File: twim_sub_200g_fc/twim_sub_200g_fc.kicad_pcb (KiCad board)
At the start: 2 copper layers, 37 x 25 mm, 41 parts, among them J1 GNSS_1, J2 GNSS_2, J3 ELRS, J4 BATTERY CONNECTOR, J5 SWD CONN, J7 VTX_CONN, J8 USB_CONN, M1 Motor_Servo, M2 Motor_Servo, M3 Motor_Servo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

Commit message: qsss
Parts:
- U1: moved to B.Cu
- moved U3 25.2 mm to (111.5, 40.8)
- moved U5 19.4 mm to (111.8, 36.9)
- moved U4 11.2 mm to (125.0, 37.6)
- moved M1 8.81 mm to (128.9, 30.0)
- moved M2 8.81 mm to (128.9, 33.6)
- moved M3 8.81 mm to (128.9, 26.4)
- moved M4 8.81 mm to (128.9, 22.8)
- moved J4 8.05 mm to (125.9, 41.0)
- moved J2 8.01 mm to (132.0, 41.0)
- moved J8 6.43 mm to (119.0, 39.0)
- moved U1 3.36 mm to (120.8, 28.0), turned to -90 degrees
- moved J5 1.40 mm to (116.0, 19.3)
- moved J1 0.38 mm to (124.0, 19.0), turned to 0 degrees
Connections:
- U1 pad 2: PWM_3 -> PWM_4
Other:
- board size 37 x 25 mm -> 27 x 25 mm

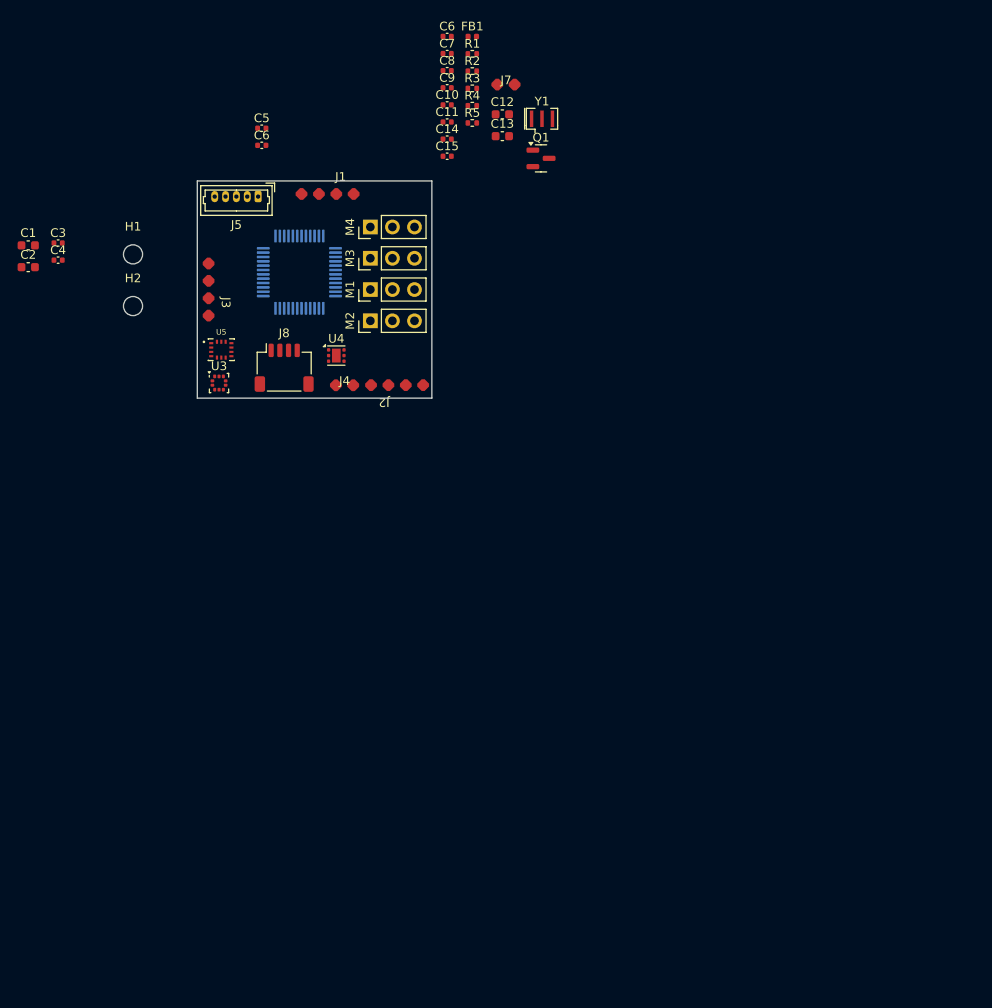
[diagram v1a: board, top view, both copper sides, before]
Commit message: added main layout 22mmx30mm
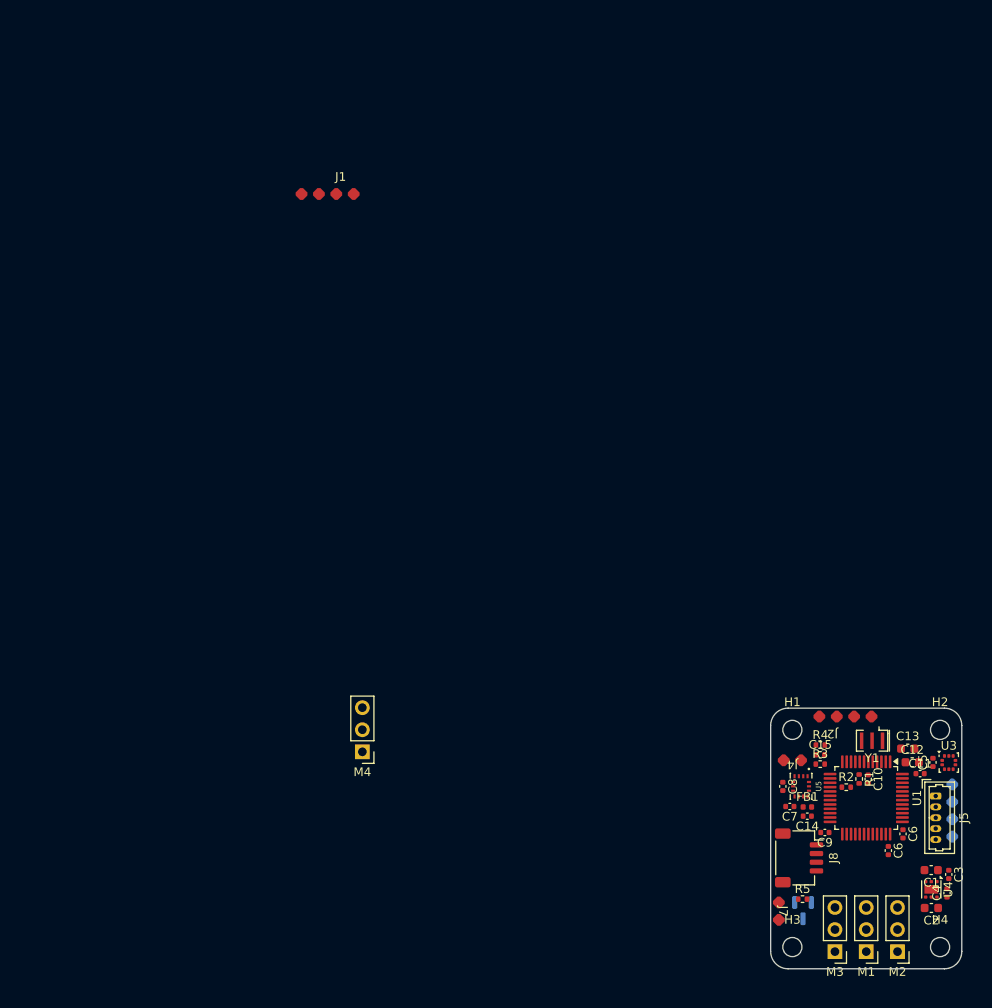
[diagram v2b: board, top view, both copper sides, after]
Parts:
- added H3: MountingHole, MountingHole:MountingHole_2.2mm_M2, F.Cu at (177.5, 105.7)
- added H4: MountingHole, MountingHole:MountingHole_2.2mm_M2, F.Cu at (194.5, 105.7)
- J3, Q1: moved to B.Cu
- U1: moved to F.Cu
- moved C2 127.5 mm to (193.5, 101.2), turned to 180 degrees
- moved C1 126.4 mm to (193.5, 96.8), turned to 180 degrees
- moved C3 125.7 mm to (195.5, 97.3), turned to -90 degrees
- moved C4 125.6 mm to (195.3, 99.5), turned to 90 degrees
- moved C6 108.3 mm to (190.2, 92.7), turned to -90 degrees
- moved C6 106.6 mm to (188.5, 94.6), turned to -90 degrees
- moved C5 106.3 mm to (193.7, 84.4), turned to 90 degrees
- moved H2 104.9 mm to (194.5, 80.7)
- moved J3 104.6 mm to (195.9, 90.0)
- moved J5 104.1 mm to (194.0, 88.3), turned to -90 degrees
- moved J7 100.2 mm to (175.9, 101.6), turned to -90 degrees
- moved R5 97.1 mm to (178.7, 100.2)
- moved FB1 96.7 mm to (179.2, 89.6)
- moved C9 96.1 mm to (181.2, 92.5), turned to 180 degrees
- moved M3 96.1 mm to (182.4, 106.2), turned to 180 degrees
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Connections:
- J2 pad 1: GNSS_2_RX -> GNSS_2_TX
- J2 pad 2: GNSS_2_TX -> GNSS_2_RX
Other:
- board size 27 x 25 mm -> 22 x 30 mm

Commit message: added baselayout
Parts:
- removed J1: GNSS_1, smd_pads:01x04_smd_pad_1.2mm
- removed M4: Motor_Servo, Connector_PinHeader_2.54mm:PinHeader_1x03_P2.54mm_Vertical
- moved J2 19.2 mm to (186.0, 98.2)
- moved C10 5.30 mm to (183.0, 82.2), turned to 90 degrees
- moved R2 4.78 mm to (188.4, 88.2), turned to 180 degrees
- moved R1 4.32 mm to (184.0, 82.2), turned to 90 degrees
- moved J5 1.89 mm to (193.9, 90.2)
- moved C6 1.46 mm to (190.0, 94.7)
- moved C1 1.14 mm to (193.5, 98.0)
- moved C4 1.14 mm to (195.3, 100.6)
- moved C2 1.14 mm to (193.5, 102.3)
- moved C3 1.14 mm to (195.5, 98.5)
- moved U4 1.14 mm to (193.5, 100.2)
- moved J3 0.83 mm to (195.6, 90.7)
- moved R5 0.57 mm to (179.2, 100.3)
- moved Q1 0.57 mm to (179.3, 101.6)
- moved J7 0.55 mm to (176.5, 101.4)
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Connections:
- U1 pad 10: GNSS_2_TX -> unconnected-(U1-PA2-Pad10)
- U1 pad 11: GNSS_2_RX -> unconnected-(U1-PA3-Pad11)
- U1 pad 2: PWM_4 -> unconnected-(U1-PC13-Pad2)
- U1 pad 31: GNSS_1_TX -> GNSS_2_TX
- U1 pad 32: GNSS_1_RX -> GNSS_2_RX
- U1 pad 8: PWM_1 -> PWM_2
- U1 pad 9: PWM_2 -> PWM_1
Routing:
- net +3V3: track 0.00 -> 74.0 mm, vias 0 -> 1
- net +5V: track 0.00 -> 40.6 mm
- net GND: track 0.00 -> 26.5 mm, vias 0 -> 13
- net PWM_2: track 0.00 -> 23.7 mm, vias 0 -> 1
- net PWM_1: track 0.00 -> 22.9 mm, vias 0 -> 1
- net NRST: track 0.00 -> 19.0 mm, vias 0 -> 1
- net VTX_ON: track 0.00 -> 17.7 mm, vias 0 -> 2
- net PWM_3: track 0.00 -> 15.2 mm, vias 0 -> 1
- net GNSS_2_TX: track 0.00 -> 12.8 mm, vias 0 -> 2
- net USB_DP: track 0.00 -> 11.2 mm, vias 0 -> 2
- net SCLK_BARO: track 0.00 -> 10.5 mm, vias 0 -> 2
- net USB_DM: track 0.00 -> 9.34 mm
- net GNSS_2_RX: track 0.00 -> 8.89 mm, vias 0 -> 2
- net BAT_VOLTAGE_ADC: track 0.00 -> 8.20 mm, vias 0 -> 2
- net CS_BARO: track 0.00 -> 7.78 mm
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- added copper zone on B.Cu, net GND
- added copper zone on F.Cu, net GND
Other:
- copper layers 2 -> 4

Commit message: adddd
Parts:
- removed Q1: AO3400A, Package_TO_SOT_SMD:SOT-23
- removed U4: TLV75533PDRV, Package_SON:WSON-6-1EP_2x2mm_P0.65mm_EP1x1.6mm
- added Q2: DMG1012T, Package_TO_SOT_SMD:SOT-523, F.Cu at (178.2, 101.3)
- added U2: AP2112K-3.3, PCM_SparkFun-Semiconductor-Standard:SOT23-5, F.Cu at (193.1, 99.5)
- moved R2 3.85 mm to (192.1, 87.2), turned to 0 degrees
- moved C1 2.69 mm to (190.8, 97.8), turned to -90 degrees
- moved R5 1.28 mm to (179.9, 101.4), turned to 90 degrees
- moved C4 1.12 mm to (195.0, 101.7)
- moved C6 0.75 mm to (189.3, 94.4), turned to 0 degrees
- moved C2 0.50 mm to (193.0, 102.4)
- moved C3 0.41 mm to (195.1, 98.4)
- moved C14 0.33 mm to (179.5, 90.8), turned to 180 degrees
- moved C11 0.24 mm to (192.1, 85.7)
- moved FB1 0.12 mm to (179.2, 89.7)
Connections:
- J2 pad 1: GNSS_2_TX -> GNSS_2_RX
- J2 pad 2: GNSS_2_RX -> GNSS_2_TX
- J3 pad 3: +5V -> GND
- J3 pad 4: GND -> +5V
- U1 pad 17: unconnected-(U1-PB1-Pad17) -> INT_DR_IMU_1
- U1 pad 18: unconnected-(U1-PB2-Pad18) -> INT_DR_IMU_2
- U1 pad 2: unconnected-(U1-PC13-Pad2) -> INT_DR_BARO
- U1 pad 25: unconnected-(U1-PB11-Pad25) -> VTX_ON
- U1 pad 39: VTX_ON -> unconnected-(U1-PA15-Pad39)
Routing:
- net +3V3: track 74.0 -> 34.9 mm, vias 1 -> 20
- net GND: track 26.5 -> 49.1 mm, vias 13 -> 31
- net +5V: track 40.6 -> 57.3 mm, vias 0 -> 9
- net INT_DR_BARO: track 0.00 -> 12.6 mm
- net INT_DR_IMU_1: track 0.00 -> 7.42 mm, vias 0 -> 2
- net GNSS_2_TX: track 12.8 -> 5.89 mm
- net VTX_ON: track 17.7 -> 12.7 mm
- net INT_DR_IMU_2: track 0.00 -> 4.39 mm
- net ELRS_RX: track 5.49 -> 9.60 mm, vias 1 -> 2
- net ELRS_TX: track 6.19 -> 9.36 mm, vias 1 -> 2
- net GNSS_2_RX: track 8.89 -> 6.40 mm
- net SCLK_BARO: track 10.5 -> 8.29 mm
- net PWM_1: track 22.9 -> 24.6 mm
- net SCLK_IMU: track 4.02 -> 5.58 mm
- net Net-(J7-Pin_2): track 3.00 -> 1.50 mm, vias 1 -> 0
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- added copper zone on In2.Cu, net +3V3
- added copper zone on In2.Cu, net +5V
- added copper zone on In1.Cu, net GND
- removed copper zone on B.Cu, net GND
- removed copper zone on F.Cu, net GND

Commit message: added tom's changes
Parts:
- removed J8: USB_CONN, Connector_JST:JST_SH_SM04B-SRSS-TB_1x04-1MP_P1.00mm_Horizontal
- added C16: 1uF, Capacitor_SMD:C_0402_1005Metric, F.Cu at (183.7, 104.9)
- added C16: 1uF, Capacitor_SMD:C_0402_1005Metric, F.Cu at (187.3, 104.9)
- added C21: 100nF, Capacitor_SMD:C_0402_1005Metric, F.Cu at (184.7, 104.9)
- added C21: 100nF, Capacitor_SMD:C_0402_1005Metric, F.Cu at (188.3, 104.9)
- added J1: Conn_JST_SH_01x04_Horizontal_SMD, PCM_fab:Conn_JST_SH_01x04_Horizontal_SMD, B.Cu at (178.2, 95.5)
- moved M1 5.03 mm to (186.0, 101.2), turned to 0 degrees
- moved M2 5.03 mm to (189.6, 101.2), turned to 0 degrees
- moved M3 5.03 mm to (182.4, 101.2), turned to 0 degrees
- moved C9 0.47 mm to (181.5, 92.9), turned to -90 degrees
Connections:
- J2 pad 3: +5V -> GND
- J2 pad 4: GND -> +5V
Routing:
- net +5V: track 57.3 -> 44.3 mm, vias 9 -> 11
- net PWM_1: track 24.6 -> 18.6 mm
- net PWM_3: track 15.1 -> 10.0 mm
- net PWM_2: track 23.9 -> 18.9 mm
- net GND: track 49.1 -> 50.2 mm, vias 31 -> 54
- net SCLK_BARO: track 8.29 -> 9.40 mm
- net +3V3: track 34.9 -> 35.8 mm, vias 20 -> 16
- net USB_DP: track 10.3 -> 10.7 mm, vias 2 -> 1
- net VTX_ON: track 12.7 -> 12.4 mm, vias 2 -> 3
- net USB_DM: track 9.89 -> 9.64 mm, vias 0 -> 1
- added copper zone on B.Cu, net +5V
- added copper zone on F.Cu, net GND

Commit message: finished V1
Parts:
- added G***: LOGO, LOGO, B.Cu at (187.0, 88.5)
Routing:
- net +5V: track 44.3 -> 43.6 mm
- net GND: track 50.2 -> 49.5 mm
- net VTX_ON: vias 3 -> 2
- added copper zone on B.Cu, net GND
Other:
- board text added: "+"
- board text added: "-"
- board text added: "1"
- board text added: "2"
- board text added: "3"
- board text added: "5V+"
- board text added: "GND"
- board text added: "RX"
- board text added: "TWIM"
- board text added: "TX"
